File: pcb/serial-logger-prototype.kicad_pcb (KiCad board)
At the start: 2 copper layers, 100 x 30 mm, 54 parts, among them J1 Conn_ARM_JTAG_SWD_10, J2 Conn_01x04_Female, J3 Conn_01x04_Female, J4 Conn_01x03_Male, SW1 Rotary_Encoder_Switch_DualLED, SW2 SW_SPDT, U1 STM32G070KBT6, U2 74LVC3G17, U3 TLV70228_SOT23-5, U4 sn74lv1t34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

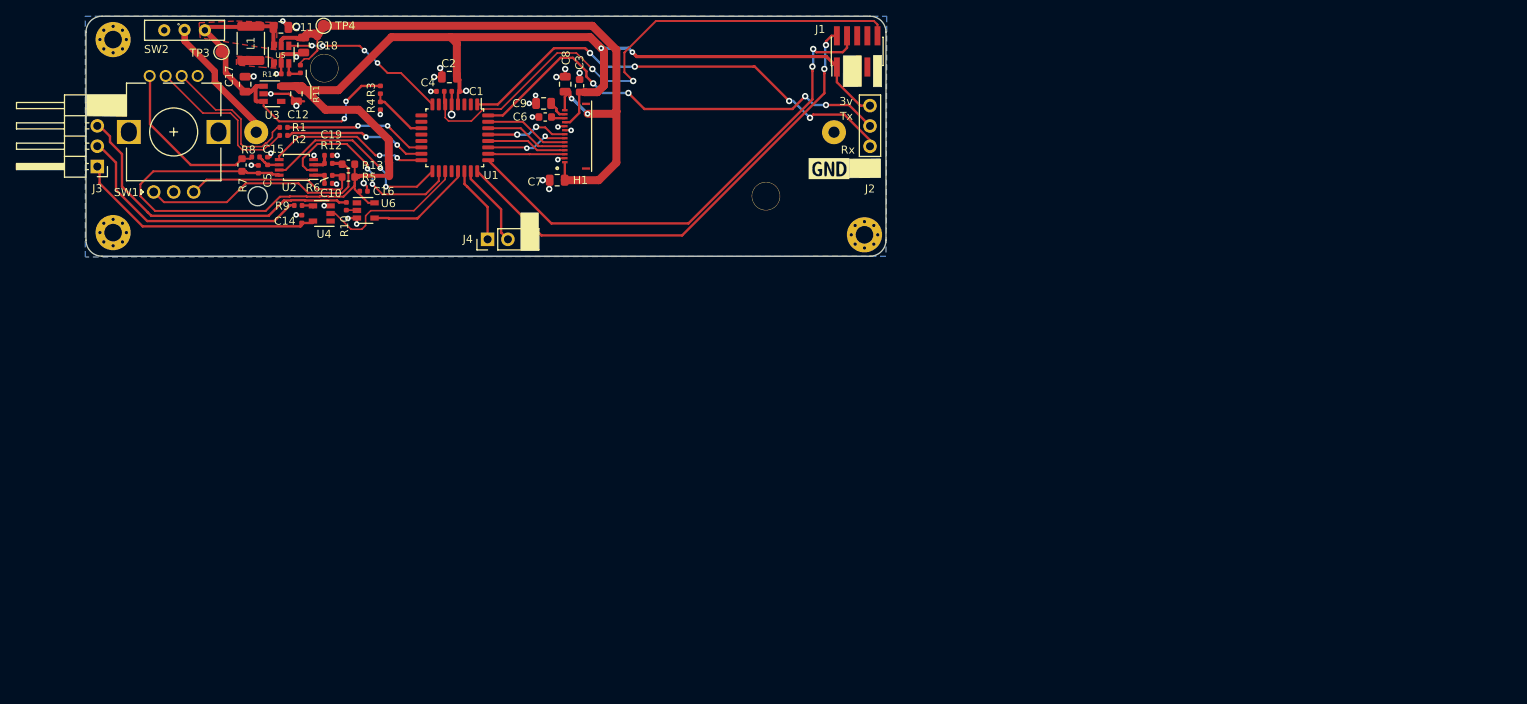
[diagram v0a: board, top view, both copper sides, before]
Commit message: PCB: cleanup layout, optimize for 3d enclosure
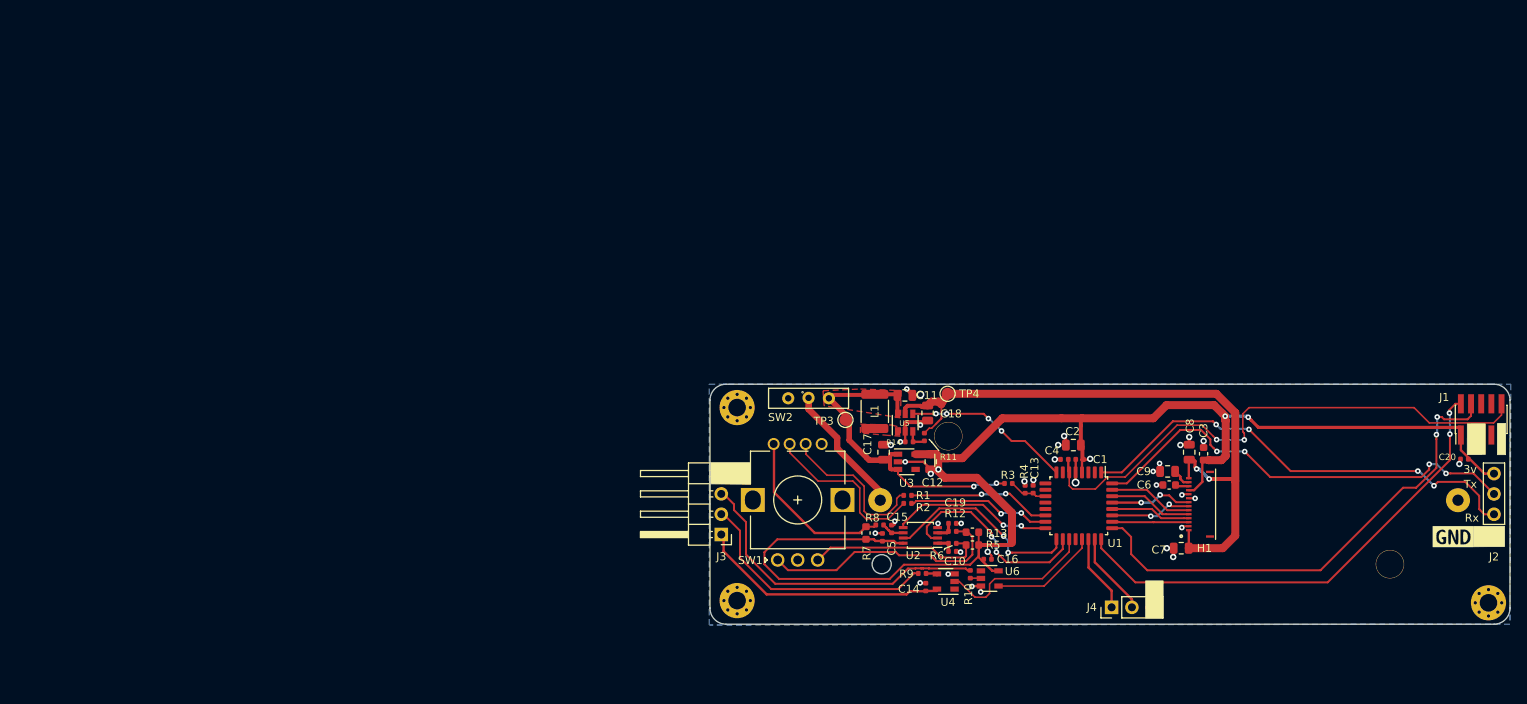
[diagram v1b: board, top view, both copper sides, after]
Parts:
- added C13: 100nF, Capacitor_SMD:C_0402_1005Metric, F.Cu at (140.4, 113.1)
- added C20: 10nF, Capacitor_SMD:C_0402_1005Metric, F.Cu at (194.3, 109.4)
- R3, R4: value 47 -> 10k
- moved R4 93.8 mm to (139.4, 113.1), turned to 270 degrees
- moved R3 92.6 mm to (137.3, 112.4), turned to 180 degrees
- moved C17 92.1 mm to (121.7, 108.5)
- moved C12 91.7 mm to (127.6, 109.7)
- moved U3 91.7 mm to (124.6, 109.7)
- moved C10 90.6 mm to (130.3, 120.9)
- moved C11 90.6 mm to (124.4, 101.4)
- moved C19 90.6 mm to (130.3, 117.4)
- moved C4 90.6 mm to (144.3, 109.4)
- moved J1 90.6 mm to (196.4, 104.4)
- moved L1 90.6 mm to (120.6, 103.4)
- moved R12 90.6 mm to (130.3, 118.4)
- moved R13 90.6 mm to (132.8, 118.5)
- moved R5 90.6 mm to (132.8, 120.1)
- moved R6 90.6 mm to (130.3, 119.9)
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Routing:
- net +BATT: track 46.2 -> 42.6 mm
- net +3V3: track 183.0 -> 179.5 mm
- net /~NRST: track 70.7 -> 68.0 mm
- net /BAT_VOLT: track 7.52 -> 4.76 mm
- net /SWDIO: track 62.3 -> 60.9 mm
- net +16V: track 83.7 -> 82.6 mm
- net /SWCLK: track 62.7 -> 61.7 mm
- net Net-(R1-Pad2): track 19.0 -> 19.9 mm
- net Net-(R2-Pad2): track 20.6 -> 21.3 mm
- net GND: track 46.3 -> 46.5 mm, vias 36 -> 39

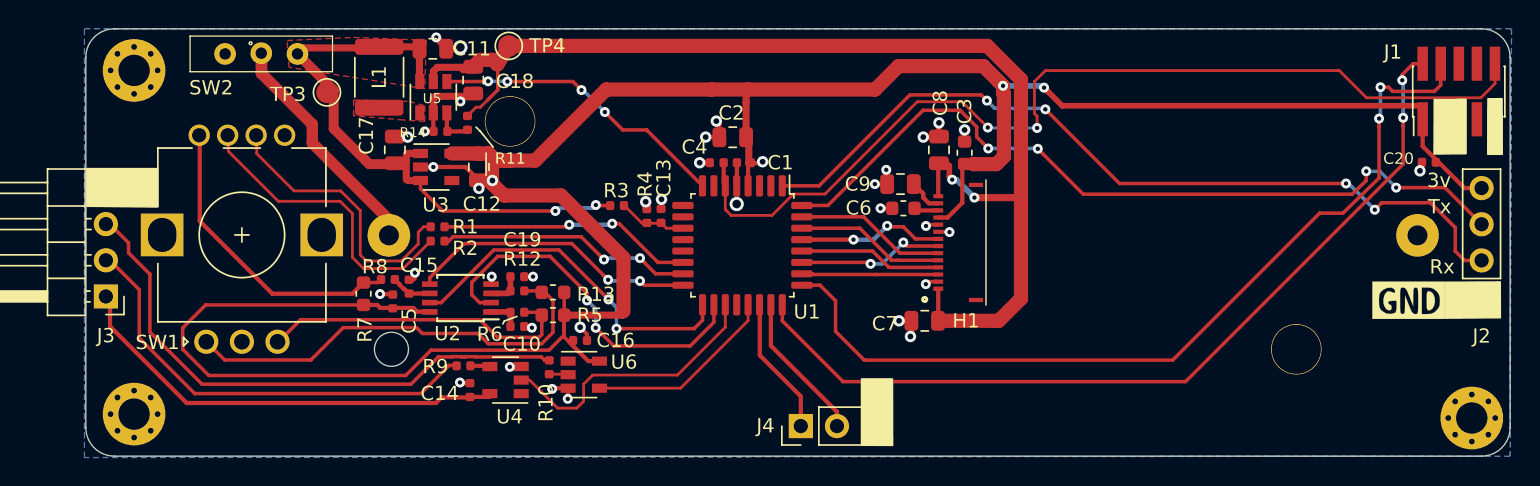
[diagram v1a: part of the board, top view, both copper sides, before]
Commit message: PCB: tweak placements + silk screen
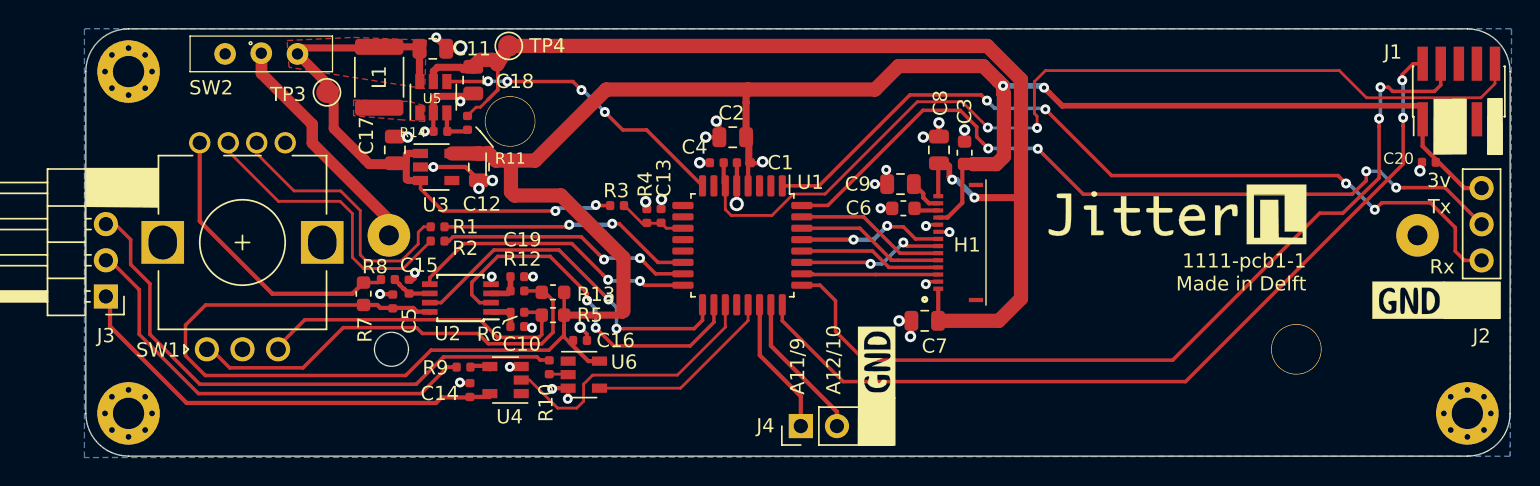
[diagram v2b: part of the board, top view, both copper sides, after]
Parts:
- added G***: LOGO, Jitter_Logos:Jitter-mini, B.Cu at (184.1, 100.9)
- added G***: LOGO, Jitter_Logos:Jitter-med, F.Cu at (176.4, 113.0)
- added G***: LOGO, Logo:GND, F.Cu at (155.5, 123.5)
- moved SW1 0.53 mm to (111.0, 115.0)
- moved H3 0.45 mm to (197.0, 127.0)
- moved H2 0.40 mm to (103.0, 103.0)
- moved H4 0.39 mm to (103.0, 127.0)
- moved R9 0.09 mm to (126.5, 123.8)
- turned G*** to 180 degrees
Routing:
- net +3V3: track 179.5 -> 177.1 mm
- net GND: track 46.5 -> 47.5 mm
- net /A: track 31.1 -> 31.7 mm
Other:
- outline, holes or cut-outs redrawn
- board text added: "1111-pcb1-1 Made in Delft"
- board text added: "A11/9"
- board text added: "A12 A11"
- board text added: "A12/10"
- board text added: "Rx Tx Vbus_in"
- board text added: "Uartwise SerialLogger V1"
- board text removed: "Vbus_in Tx Rx"

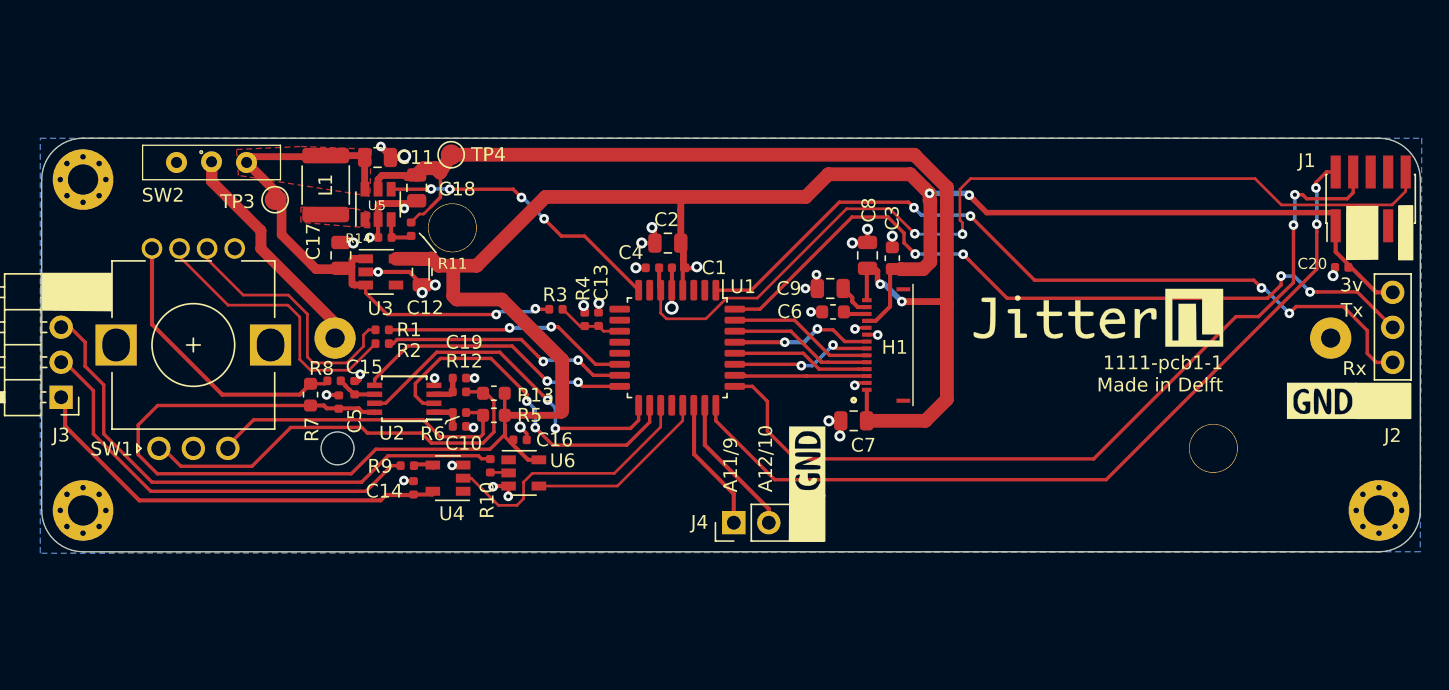
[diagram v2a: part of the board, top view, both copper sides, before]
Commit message: PCB: finalize design (DRC pass)
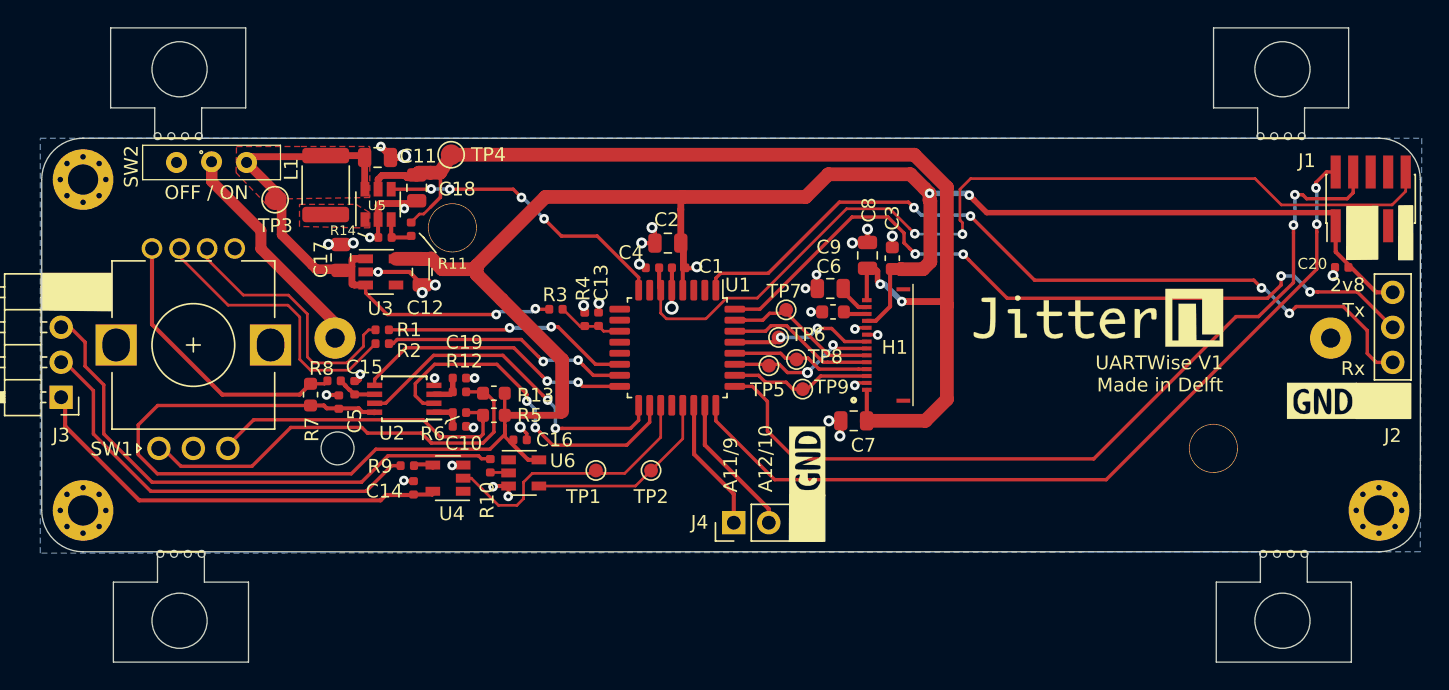
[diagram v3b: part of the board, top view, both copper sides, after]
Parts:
- added MB1: MouseBite, Jitter_Footprints:MouseBite_3.5mmx2.2mm_breakaway, F.Cu at (108.2, 100.0)
- added MB2: MouseBite, Jitter_Footprints:MouseBite_3.5mmx2.2mm_breakaway, F.Cu at (111.8, 130.0)
- added MB3: MouseBite, Jitter_Footprints:MouseBite_3.5mmx2.2mm_breakaway, F.Cu at (188.2, 100.0)
- added MB4: MouseBite, Jitter_Footprints:MouseBite_3.5mmx2.2mm_breakaway, F.Cu at (191.8, 130.0)
- added TH1: ToolingHole, Jitter_Footprints:Tooling_hole_4mm_4.04mm_paste, F.Cu at (110.0, 95.0)
- added TH2: ToolingHole, Jitter_Footprints:Tooling_hole_4mm_4.04mm_paste, F.Cu at (110.0, 135.0)
- added TH3: ToolingHole, Jitter_Footprints:Tooling_hole_4mm_4.04mm_paste, F.Cu at (190.0, 95.0)
- added TH4: ToolingHole, Jitter_Footprints:Tooling_hole_4mm_4.04mm_paste, F.Cu at (190.0, 135.0)
- added TP1: TestPoint, TestPoint:TestPoint_Pad_D1.0mm, F.Cu at (140.2, 124.1)
- added TP2: TestPoint, TestPoint:TestPoint_Pad_D1.0mm, F.Cu at (144.2, 124.1)
- added TP5: TestPoint, TestPoint:TestPoint_Pad_D1.0mm, F.Cu at (152.8, 116.5)
- added TP6: TestPoint, TestPoint:TestPoint_Pad_D1.0mm, F.Cu at (153.4, 114.5)
- added TP7: TestPoint, TestPoint:TestPoint_Pad_D1.0mm, F.Cu at (154.0, 112.5)
- added TP8: TestPoint, TestPoint:TestPoint_Pad_D1.0mm, F.Cu at (154.8, 116.0)
- added TP9: TestPoint, TestPoint:TestPoint_Pad_D1.0mm, F.Cu at (155.2, 118.2)
- moved C17 0.15 mm to (121.7, 108.7)
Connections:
- net +3V3 renamed +2V8
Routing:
- net +2V8: track 177.1 -> 174.8 mm
- net /TX1: track 19.8 -> 20.8 mm
- net GND: track 47.5 -> 48.5 mm, vias 39 -> 40
- net /FRAME_SYNC: track 9.60 -> 10.6 mm
- net /RX1: track 13.6 -> 14.4 mm
- net /16V_enable: track 21.0 -> 21.5 mm
- net /DEBUG_RX3: track 57.9 -> 58.5 mm
- net /SPI1_SCLK: track 10.3 -> 10.8 mm
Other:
- board size 100 x 30 mm -> 100 x 46 mm
- rule pad_to_mask_clearance: 0.051 -> 0.05
- rule solder_mask_min_width: 0.25 -> 0.08
- board text added: "2v8"
- board text added: "OFF / ON"
- board text added: "UARTWise V1"
- board text added: "UARTWise V1 Made in Delft"
- board text removed: "1111-pcb1-1 Made in Delft"
- board text removed: "3v"
- board text removed: "Uartwise SerialLogger V1"
